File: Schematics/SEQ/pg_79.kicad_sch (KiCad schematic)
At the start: 39 parts, among them U8007 F02, U8008 F02, U8009 F02, U8010 F02, U8012 F37, U8013 F37, U8016 F37, U8018 F04, U8019 F64, U8020 F04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

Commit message: KiCad 6
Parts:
- GB226, GB274, GB275, GB276, GB277, GB278, GB284, GB301, GB302, GB303, GB305, GB306, GB307, GB308, GB311, GB312, GB313, GB314: value GB -> (none)
- U8007, U8008, U8009, U8010, U8021, U8033, U8035: value F02 -> (none)
- U8012, U8013, U8016: value F37 -> (none)
- U8018, U8020, U8029: value F04 -> (none)
- U8019: value F64 -> (none)
- U8022, U8025, U8026, U8027: value F20 -> (none)
- U8028: value F00 -> (none)
- U8030: value F30 -> (none)
- U8034: value F74 -> (none)

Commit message: Recover from KiCad-6 munging
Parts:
- GB226, GB274, GB275, GB276, GB277, GB278, GB284, GB301, GB302, GB303, GB305, GB306, GB307, GB308, GB311, GB312, GB313, GB314: value (none) -> GB
- U8007, U8008, U8009, U8010, U8021, U8033, U8035: value (none) -> F02
- U8012, U8013, U8016: value (none) -> F37
- U8018, U8020, U8029: value (none) -> F04
- U8019: value (none) -> F64
- U8022, U8025, U8026, U8027: value (none) -> F20
- U8028: value (none) -> F00
- U8030: value (none) -> F30
- U8034: value (none) -> F74

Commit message: Use "bidirectional" as intended.
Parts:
- removed GB301, GB305, GB306, GB311: GB, symbol r1000:GB
- added GB309, GB310: GB, symbol r1000:GB
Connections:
- net LOCL_STOP.DIAG~: no longer U8025.1 (D0)
- net PREDECODE.FSM: now also U8010.2 (D1); no longer U8010.1 (D0)
- net PU: now also U8025.1 (D0)
- net SF_STOP: now also U8010.1 (D0); no longer U8010.2 (D1)
- new net H1: GB309.1
- new net H2: GB310.1
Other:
- moved on the sheet: U8007, U8010, U8016, U8020, U8021, U8022, U8025, U8026, U8027, U8028, U8029

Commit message: Snapshot
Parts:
- added GB311: GB, symbol r1000:GB
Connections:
- new net Q1~: GB311.1
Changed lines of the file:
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@@
   (wire (pts (xy 25.4 124.46) (xy 50.8 124.46) ) )
   (wire (pts (xy 25.4 137.16) (xy 50.8 137.16) ) )
+  (wire (pts (xy 25.4 149.86) (xy 50.8 149.86) ) )
   (wire (pts (xy 25.4 162.56) (xy 50.8 162.56) ) )
   (wire (pts (xy 25.4 175.26) (xy 58.42 175.26) ) )
@@
   (symbol (lib_id "r1000:GB") (at 25.4 124.46 0) (mirror y) (unit 1) (in_bom yes) (on_board yes) (property "Reference" "GB309" (id 0) (at 21.59 124.46 0) (effects (font (size 2.54 2.54) ) (justify left) ) ) (property "Value" "GB" (id 1) (at 25.4 124.46 0) (effects (font (size 1.27 1.27) ) hide ) ) (property "Footprint" "" (id 2) (at 25.4 124.46 0) (effects (font (size 1.27 1.27) ) hide ) ) (property "Datasheet" "" (id 3) (at 25.4 124.46 0) (effects (font (size 1.27 1.27) ) hide ) ) (pin "1") )
   (symbol (lib_id "r1000:GB") (at 25.4 137.16 0) (mirror y) (unit 1) (in_bom yes) (on_board yes) (property "Reference" "GB310" (id 0) (at 21.59 137.16 0) (effects (font (size 2.54 2.54) ) (justify left) ) ) (property "Value" "GB" (id 1) (at 25.4 137.16 0) (effects (font (size 1.27 1.27) ) hide ) ) (property "Footprint" "" (id 2) (at 25.4 137.16 0) (effects (font (size 1.27 1.27) ) hide ) ) (property "Datasheet" "" (id 3) (at 25.4 137.16 0) (effects (font (size 1.27 1.27) ) hide ) ) (pin "1") )
+  (symbol (lib_id "r1000:GB") (at 25.4 149.86 0) (mirror y) (unit 1) (in_bom yes) (on_board yes) (property "Reference" "GB311" (id 0) (at 21.59 149.86 0) (effects (font (size 2.54 2.54) ) (justify left) ) ) (property "Value" "GB" (id 1) (at 25.4 149.86 0) (effects (font (size 1.27 1.27) ) hide ) ) (property "Footprint" "" (id 2) (at 25.4 149.86 0) (effects (font (size 1.27 1.27) ) hide ) ) (property "Datasheet" "" (id 3) (at 25.4 149.86 0) (effects (font (size 1.27 1.27) ) hide ) ) (pin "1") )
   (symbol (lib_id "r1000:GB") (at 25.4 162.56 0) (mirror y) (unit 1) (in_bom yes) (on_board yes) (property "Reference" "GB312" (id 0) (at 21.59 162.56 0) (effects (font (size 2.54 2.54) ) (justify left) ) ) (property "Value" "GB" (id 1) (at 25.4 162.56 0) (effects (font (size 1.27 1.27) ) hide ) ) (property "Footprint" "" (id 2) (at 25.4 162.56 0) (effects (font (size 1.27 1.27) ) hide ) ) (property "Datasheet" "" (id 3) (at 25.4 162.56 0) (effects (font (size 1.27 1.27) ) hide ) ) (pin "1") )
   (symbol (lib_id "r1000:GB") (at 25.4 175.26 0) (mirror y) (unit 1) (in_bom yes) (on_board yes) (property "Reference" "GB313" (id 0) (at 21.59 175.26 0) (effects (font (size 2.54 2.54) ) (justify left) ) ) (property "Value" "GB" (id 1) (at 25.4 175.26 0) (effects (font (size 1.27 1.27) ) hide ) ) (property "Footprint" "" (id 2) (at 25.4 175.26 0) (effects (font (size 1.27 1.27) ) hide ) ) (property "Datasheet" "" (id 3) (at 25.4 175.26 0) (effects (font (size 1.27 1.27) ) hide ) ) (pin "1") )
@@
   (global_label "H1" (shape output) (at 50.8 124.46 0) (fields_autoplaced) (effects (font (size 2.54 2.54) ) (justify left) ) (property "Intersheet References" "${INTERSHEET_REFS}" (id 0) (at 61.5634 124.46 0) (effects (font (size 1.905 1.905) ) (justify left) ) ) )
   (global_label "H2" (shape output) (at 50.8 137.16 0) (fields_autoplaced) (effects (font (size 2.54 2.54) ) (justify left) ) (property "Intersheet References" "${INTERSHEET_REFS}" (id 0) (at 61.5634 137.16 0) (effects (font (size 1.905 1.905) ) (justify left) ) ) )
+  (global_label "Q1~" (shape output) (at 50.8 149.86 0) (fields_autoplaced) (effects (font (size 2.54 2.54) ) (justify left) ) (property "Intersheet References" "${INTERSHEET_REFS}" (id 0) (at 63.3777 149.86 0) (effects (font (size 1.905 1.905) ) (justify left) ) ) )
   (global_label "Q2~" (shape output) (at 50.8 162.56 0) (fields_autoplaced) (effects (font (size 2.54 2.54) ) (justify left) ) (property "Intersheet References" "${INTERSHEET_REFS}" (id 0) (at 62.5203 162.4013 0) (effects (font (size 1.905 1.905) ) (justify left) ) ) )
   (label "Q3~" (at 50.8 175.26 0) (effects (font (size 2.54 2.54) ) (justify left bottom) ) )

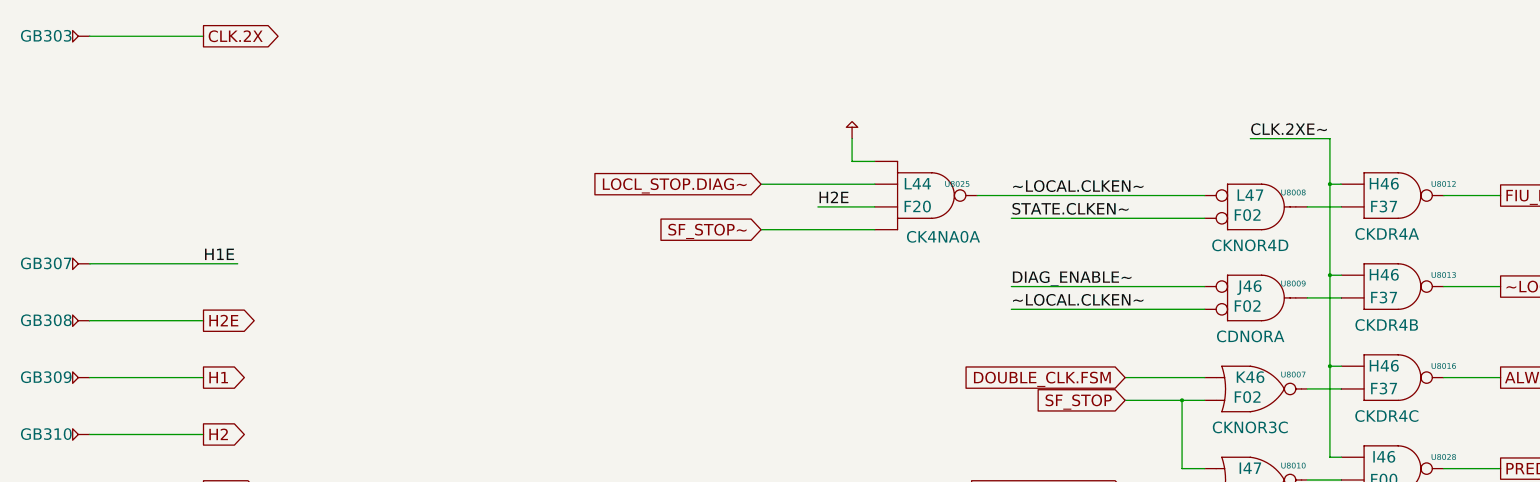
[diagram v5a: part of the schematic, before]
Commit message: Snapshot with some significant speedups.
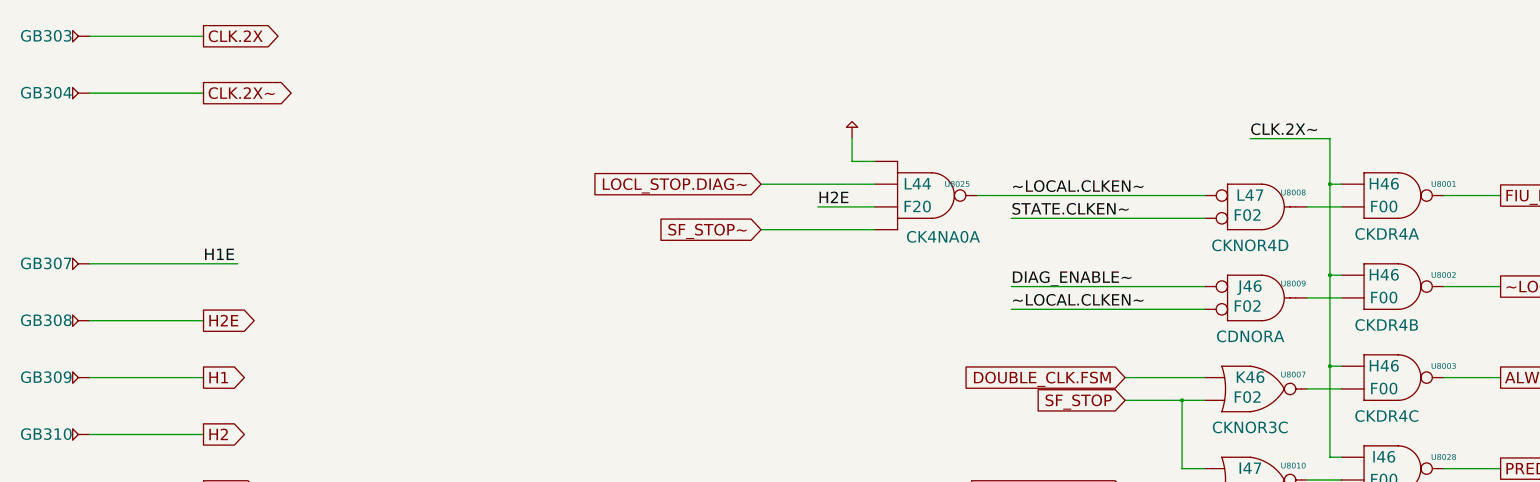
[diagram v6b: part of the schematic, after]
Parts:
- removed U8012, U8013, U8016: F37, symbol r1000:F37
- added GB304: GB, symbol r1000:GB
- added U8001, U8002, U8003: F00, symbol r1000:F00
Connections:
- net ALWAYS.CLK~: now also U8003.3 (Q)
- net CLK.2XE~: no longer U8028.1 (D0)
- net FIU_REG.CLK~: now also U8001.3 (Q)
- net ~LOCAL.CLK~: now also U8002.3 (Q)
- net at U8007.3 (Q): now also U8003.2 (D1)
- net at U8008.3 (Q): now also U8001.2 (D1)
- net at U8009.3 (Q): now also U8002.2 (D1)
- new net CLK.2X~: GB304.1, U8001.1 (D0), U8002.1 (D0), U8003.1 (D0), U8028.1 (D0)

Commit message: Fix polarity of unused part of driven FIU bus.
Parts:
- removed GB226, GB274, GB275, GB276, GB277, GB278, GB284, GB302, GB303, GB304, GB307, GB308, GB309, GB310, GB311, GB312, GB313, GB314: GB, symbol r1000:GB
- removed U8001, U8002, U8003, U8028: F00, symbol r1000:F00
- removed U8007, U8008, U8009, U8010, U8021, U8033, U8035: F02, symbol r1000:F02
- removed U8018, U8020, U8029: F04, symbol r1000:F04
- removed U8019: F64, symbol r1000:F64
- removed U8022, U8025, U8026, U8027: F20, symbol r1000:F20
- removed U8030: F30, symbol r1000:F30
- removed U8034: F74, symbol r1000:F74
- added U (x18): (no value), symbol r1000:GB
- added U (x3): (no value), symbol r1000:F04
- added U (x4): (no value), symbol r1000:F00
- added U (x7): (no value), symbol r1000:F02
- added U: (no value), symbol r1000:F30
- added U (x4): (no value), symbol r1000:F20
- added U: (no value), symbol r1000:F74
- added U: (no value), symbol r1000:F64
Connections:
- net ALWAYS.CLK~: now also U.3 (Q)
- net BAD_HINT.CLKEN~: now also U.6 (Q)
- net CLK.2X: now also U.1
- net CLK.2XE~: now also U.1, U.3 (CLK)
- net CLK.2X~: now also U.1, U.1 (D0), U.1 (D0), U.1 (D0), U.1 (D0)
- net DIAG.FORCE_CLK: now also U.2 (D1)
- net DIAG_ENABLE: now also U.4 (D2), U.4 (D2), U.4 (D2), U.5 (Q)
- net DIAG_ENABLE~: now also U.1 (D0), U.6 (Q_)
- net DIAG_STOP: now also U.2 (D1)
- net DOUBLE_CLK.FSM: now also U.1 (D0)
- net FIU_REG.CLK~: now also U.3 (Q)
- net H1: now also U.1
- net H1E: now also U.1, U.1 (D0)
- net H2: now also U.1
- net H2E: now also U.1, U.1 (D0), U.1 (D0), U.1 (D0), U.4 (D2)
- net LOCL_STOP.DIAG~: now also U.2 (D1)
- net L_MACRO_HIC: now also U.2 (D1)
- net L_MACRO_HIC~: now also U.5 (D3)
- net MICRO_EVENT: now also U.1 (D0)
- net MICRO_STOP: now also U.6 (C2), U.8 (Q)
- net PREDECODE.CLK~: now also U.3 (Q)
- net PREDECODE.FSM: now also U.2 (D1)
- net PU: now also U.1 (CL_), U.1 (D0), U.13 (D3), U.4 (C0), U.4 (PR_), U.5 (D6), U.6 (D7)
- net Q.ECC_CLKSTOP: now also U.1, U.1 (D0)
- net Q.ECC_STOP.EN: now also U.1
- net Q.ECC_STOP_REGD: now also U.11 (D1)
- net Q.STOP~0: now also U.1, U.11 (D0)
- net Q.STOP~1: now also U.1, U.12 (D1)
- net Q.STOP~2: now also U.1, U.1 (D2)
- net Q.STOP~3: now also U.1, U.2 (D3)
- net Q.STOP~4: now also U.1, U.3 (D4)
- net Q.STOP~5: now also U.4 (D5)
- net Q1~: now also U.1
- net Q2~: now also U.1
- net Q3: now also U.10 (B1), U.12 (D2), U.3 (Q), U.5 (C1)
- net Q3~: now also U.1, U.1 (D0), U.3 (A1)
- net Q4~: now also U.1
- net SEQ_STOP: now also U.1 (D0)
- net SEQ_STOP~: now also U.2 (Q), U.5 (D3)
- net SF_STOP: now also U.1 (D0), U.2 (D1), U.9 (B0)
- net SF_STOP~: now also U.5 (D3)
- net STACK.CLKEN~: now also U.6 (Q)
- net STATE.CLKEN: now also U.2 (Q)
- net STATE.CLKEN~: now also U.1 (D0), U.2 (D1), U.6 (Q)
- net STATE_STOP: now also U.2 (A0), U.2 (Q)
- net STATE_STOP~: now also U.1 (D0), U.2 (D1), U.2 (D1), U.2 (D1), U.8 (Q)
- net ~LOCAL.CLKEN~: now also U.1 (D0), U.2 (D1), U.6 (Q)
- net ~LOCAL.CLK~: now also U.3 (Q)
- new net: U.2 (D1), U.3 (Q) (x4)
- new net: U.3 (Q), U.5 (D3)
- new net: U.2 (D), U.3 (Q)

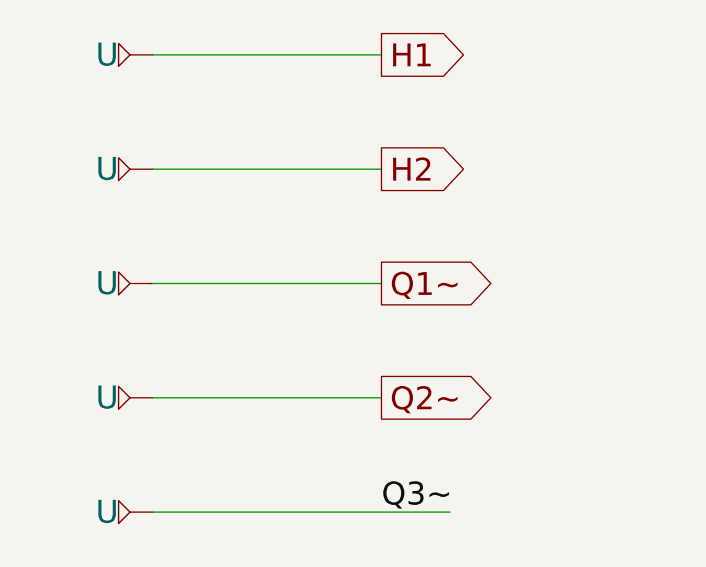
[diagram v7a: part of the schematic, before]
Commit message: Fix WCS parity
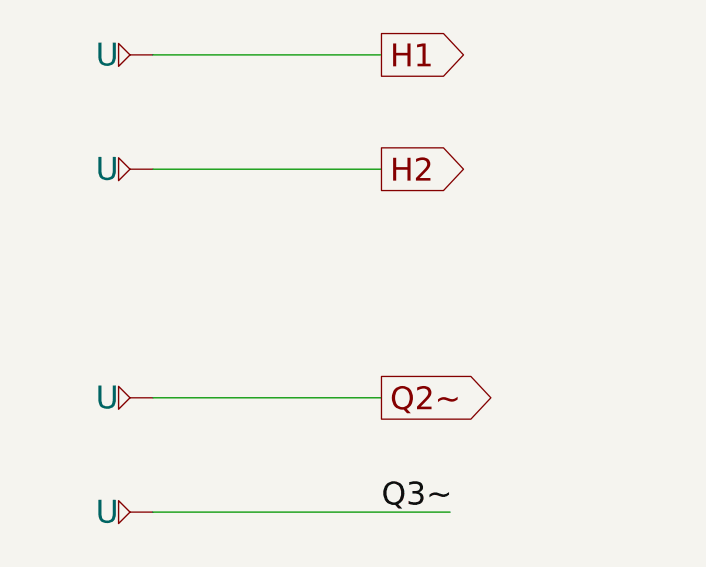
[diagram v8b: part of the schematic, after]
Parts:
- removed U: (no value), symbol r1000:GB
